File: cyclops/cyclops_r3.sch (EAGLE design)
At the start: 135 parts, among them Q1 BC817, Q2 IRF510, U1 MCP4921, U10 TLV2374, U11 THS4281, U12 MAX4564, U13 ZXTD, U14 ZXTD, U2 ADG3301, U3 MCP4022-50k, U4 LT1931, U5 LT1963A, U6 337L, U7 TLV3701, U8 ADR03, U9 OP1177, X1 SLP3, X2 SLP3, X3 SLP3

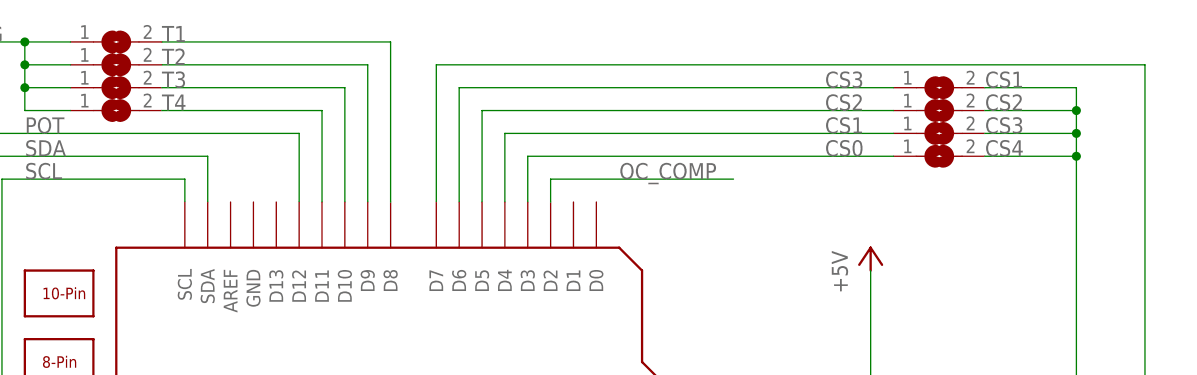
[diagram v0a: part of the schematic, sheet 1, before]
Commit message: Refixed the incorrect labels on the jumper pads.
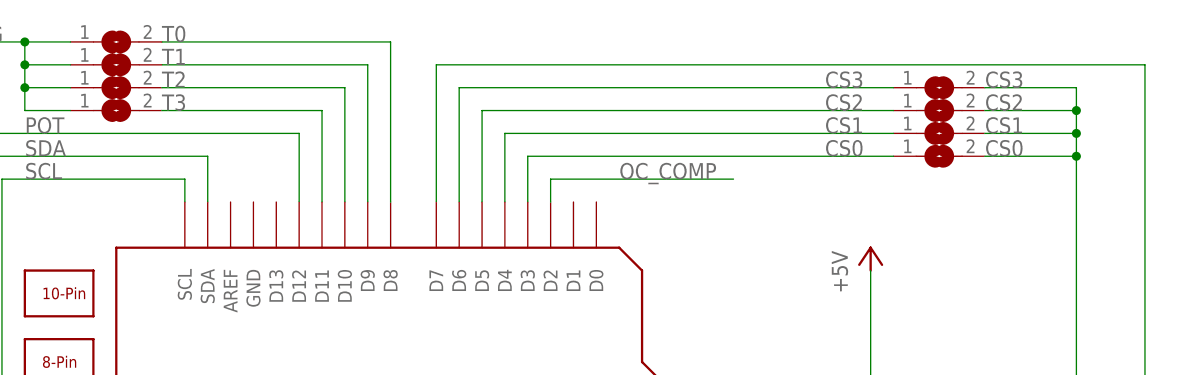
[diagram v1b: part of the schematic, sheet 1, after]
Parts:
- removed T4: (no value), cyclops:SJ
- added T0: (no value), cyclops:SJ
- renumbered CS4 to CS0
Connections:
- net CS1: now also CS1.1; no longer CS3.1
- net CS3: now also CS3.1; no longer CS1.1
- net T0: now also T0.2; no longer T1.2
- net T1: now also T1.2; no longer T2.2
- net T2: now also T2.2; no longer T3.2
- net T3: now also T3.2; no longer T4.2
- net TRIG: now also T0.1; no longer T4.1
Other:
- moved on the sheet: CS1, CS3, T1, T2, T3
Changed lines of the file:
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@@
 <part name="C28" library="cyclops" deviceset="C" device="_0805" value="1uF"/>
 <part name="C26" library="cyclops" deviceset="C" device="_0603" value=".1uF"/>
+<part name="CS3" library="cyclops" deviceset="SJ" device=""/>
+<part name="CS2" library="cyclops" deviceset="SJ" device=""/>
 <part name="CS1" library="cyclops" deviceset="SJ" device=""/>
-<part name="CS2" library="cyclops" deviceset="SJ" device=""/>
-<part name="CS3" library="cyclops" deviceset="SJ" device=""/>
-<part name="CS4" library="cyclops" deviceset="SJ" device=""/>
+<part name="CS0" library="cyclops" deviceset="SJ" device=""/>
 <part name="Q1" library="cyclops" deviceset="BC817*" device="SMD" technology="-16" value="BC817"/>
 <part name="R14" library="cyclops" deviceset="R" device="_0603" value="10k"/>
@@
 <part name="P-2" library="cyclops" deviceset="-5V" device="" value="-1.25V"/>
 <part name="R25" library="cyclops" deviceset="R" device="_0603" value="220k"/>
+<part name="T0" library="cyclops" deviceset="SJ" device=""/>
 <part name="T1" library="cyclops" deviceset="SJ" device=""/>
 <part name="T2" library="cyclops" deviceset="SJ" device=""/>
 <part name="T3" library="cyclops" deviceset="SJ" device=""/>
-<part name="T4" library="cyclops" deviceset="SJ" device=""/>
 <part name="TRIG" library="cyclops" deviceset="BNC" device="_V-BITE" value="361V509E"/>
 <part name="U$47" library="cyclops" deviceset="GND1" device=""/>
@@
 <instance part="TEST" gate="G$1" x="203.2" y="48.26" rot="R180"/>
 <instance part="VAUX_OUT" gate="G$1" x="109.22" y="20.32"/>
-<instance part="CS1" gate="1" x="109.22" y="127" smashed="yes">
+<instance part="CS3" gate="1" x="109.22" y="127" smashed="yes">
 <attribute name="NAME" x="114.3" y="127" size="1.778" layer="95"/>
 <attribute name="VALUE" x="106.68" y="123.19" size="1.778" layer="96"/>
@@
 <attribute name="VALUE" x="106.68" y="120.65" size="1.778" layer="96"/>
 </instance>
-<instance part="CS3" gate="1" x="109.22" y="121.92" smashed="yes">
+<instance part="CS1" gate="1" x="109.22" y="121.92" smashed="yes">
 <attribute name="NAME" x="114.3" y="121.92" size="1.778" layer="95"/>
 <attribute name="VALUE" x="106.68" y="118.11" size="1.778" layer="96"/>
 </instance>
-<instance part="CS4" gate="1" x="109.22" y="119.38" smashed="yes">
+<instance part="CS0" gate="1" x="109.22" y="119.38" smashed="yes">
 <attribute name="NAME" x="114.3" y="119.38" size="1.778" layer="95"/>
 <attribute name="VALUE" x="106.68" y="115.57" size="1.778" layer="96"/>
@@
 <instance part="U$42" gate="G$1" x="172.72" y="58.42"/>
 <instance part="U$43" gate="G$1" x="195.58" y="58.42"/>
-<instance part="T1" gate="1" x="17.78" y="132.08" smashed="yes">
+<instance part="T0" gate="1" x="17.78" y="132.08" smashed="yes">
 <attribute name="NAME" x="22.86" y="132.08" size="1.778" layer="95"/>
 <attribute name="VALUE" x="15.24" y="128.27" size="1.778" layer="96"/>
 </instance>
-<instance part="T2" gate="1" x="17.78" y="129.54" smashed="yes">
+<instance part="T1" gate="1" x="17.78" y="129.54" smashed="yes">
 <attribute name="NAME" x="22.86" y="129.54" size="1.778" layer="95"/>
 <attribute name="VALUE" x="15.24" y="125.73" size="1.778" layer="96"/>
 </instance>
-<instance part="T3" gate="1" x="17.78" y="127" smashed="yes">
+<instance part="T2" gate="1" x="17.78" y="127" smashed="yes">
 <attribute name="NAME" x="22.86" y="127" size="1.778" layer="95"/>
 <attribute name="VALUE" x="15.24" y="123.19" size="1.778" layer="96"/>
 </instance>
-<instance part="T4" gate="1" x="17.78" y="124.46" smashed="yes">
+<instance part="T3" gate="1" x="17.78" y="124.46" smashed="yes">
 <attribute name="NAME" x="22.86" y="124.46" size="1.778" layer="95"/>
 <attribute name="VALUE" x="15.24" y="120.65" size="1.778" layer="96"/>
@@
 <segment>
 <label x="96.52" y="119.38" size="1.778" layer="95"/>
-<pinref part="CS4" gate="1" pin="1"/>
+<pinref part="CS0" gate="1" pin="1"/>
 <pinref part="LEONARDO" gate="G$1" pin="D3"/>
 <wire x1="63.5" y1="119.38" x2="104.14" y2="119.38" width="0.1524" layer="91"/>
@@
 <segment>
 <label x="96.52" y="121.92" size="1.778" layer="95"/>
-<pinref part="CS3" gate="1" pin="1"/>
+<pinref part="CS1" gate="1" pin="1"/>
 <pinref part="LEONARDO" gate="G$1" pin="D4"/>
 <wire x1="60.96" y1="121.92" x2="104.14" y2="121.92" width="0.1524" layer="91"/>
@@
 <segment>
 <label x="96.52" y="127" size="1.778" layer="95"/>
-<pinref part="CS1" gate="1" pin="1"/>
+<pinref part="CS3" gate="1" pin="1"/>
 <pinref part="LEONARDO" gate="G$1" pin="D6"/>
 <wire x1="55.88" y1="127" x2="104.14" y2="127" width="0.1524" layer="91"/>
@@
 <wire x1="114.3" y1="119.38" x2="124.46" y2="119.38" width="0.1524" layer="91"/>
 <junction x="124.46" y="119.38"/>
-<pinref part="CS4" gate="1" pin="2"/>
+<pinref part="CS0" gate="1" pin="2"/>
+<pinref part="CS1" gate="1" pin="2"/>
+<pinref part="CS2" gate="1" pin="2"/>
 <pinref part="CS3" gate="1" pin="2"/>
-<pinref part="CS2" gate="1" pin="2"/>
-<pinref part="CS1" gate="1" pin="2"/>
 </segment>
 <segment>
@@
 <segment>
 <wire x1="0" y1="132.08" x2="7.62" y2="132.08" width="0.1524" layer="91"/>
+<pinref part="T0" gate="1" pin="1"/>
 <pinref part="T1" gate="1" pin="1"/>
-<pinref part="T2" gate="1" pin="1"/>
 <wire x1="7.62" y1="132.08" x2="12.7" y2="132.08" width="0.1524" layer="91"/>
 <wire x1="12.7" y1="129.54" x2="7.62" y2="129.54" width="0.1524" layer="91"/>
 <wire x1="7.62" y1="129.54" x2="7.62" y2="132.08" width="0.1524" layer="91"/>
 <junction x="7.62" y="132.08"/>
-<pinref part="T3" gate="1" pin="1"/>
+<pinref part="T2" gate="1" pin="1"/>
 <wire x1="12.7" y1="127" x2="7.62" y2="127" width="0.1524" layer="91"/>
 <wire x1="7.62" y1="127" x2="7.62" y2="129.54" width="0.1524" layer="91"/>
 <junction x="7.62" y="129.54"/>
-<pinref part="T4" gate="1" pin="1"/>
+<pinref part="T3" gate="1" pin="1"/>
 <wire x1="12.7" y1="124.46" x2="7.62" y2="124.46" width="0.1524" layer="91"/>
 <wire x1="7.62" y1="124.46" x2="7.62" y2="127" width="0.1524" layer="91"/>
@@
 <net name="T0" class="0">
 <segment>
-<pinref part="T1" gate="1" pin="2"/>
+<pinref part="T0" gate="1" pin="2"/>
 <wire x1="22.86" y1="132.08" x2="48.26" y2="132.08" width="0.1524" layer="91"/>
 <pinref part="LEONARDO" gate="G$1" pin="D8"/>
@@
 <net name="T1" class="0">
 <segment>
-<pinref part="T2" gate="1" pin="2"/>
+<pinref part="T1" gate="1" pin="2"/>
 <wire x1="22.86" y1="129.54" x2="45.72" y2="129.54" width="0.1524" layer="91"/>
 <pinref part="LEONARDO" gate="G$1" pin="D9"/>
@@
 <net name="T2" class="0">
 <segment>
-<pinref part="T3" gate="1" pin="2"/>
+<pinref part="T2" gate="1" pin="2"/>
 <wire x1="22.86" y1="127" x2="43.18" y2="127" width="0.1524" layer="91"/>
 <pinref part="LEONARDO" gate="G$1" pin="D10"/>
@@
 <net name="T3" class="0">
 <segment>
-<pinref part="T4" gate="1" pin="2"/>
+<pinref part="T3" gate="1" pin="2"/>
 <wire x1="22.86" y1="124.46" x2="40.64" y2="124.46" width="0.1524" layer="91"/>
 <pinref part="LEONARDO" gate="G$1" pin="D11"/>

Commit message: BOM simplification.
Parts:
- C4: device cyclops:C_0805 -> cyclops:C_1206
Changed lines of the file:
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@@
 <part name="LEONARDO" library="cyclops" deviceset="LEONARDO_R3_ICSP" device="" value="LEONARDO_R3_ICSP"/>
 <part name="U1" library="cyclops" deviceset="MCP4921" device="SOIC" value="MCP4921"/>
-<part name="C4" library="cyclops" deviceset="C" device="_0805" value="10uF"/>
+<part name="C4" library="cyclops" deviceset="C" device="_1206" value="10uF"/>
 <part name="C5" library="cyclops" deviceset="C" device="_0603" value=".1uF"/>
 <part name="C6" library="cyclops" deviceset="C" device="_0805" value="1uF"/>

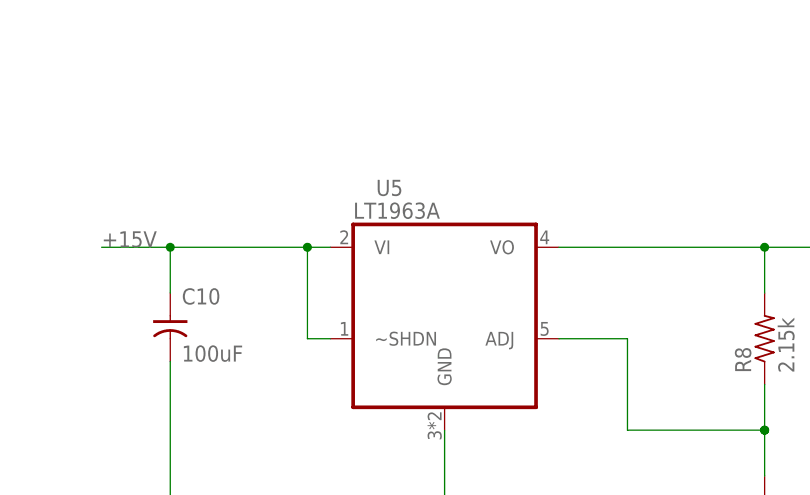
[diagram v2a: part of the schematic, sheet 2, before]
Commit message: Replaced LT1963 with LT1764 to increase current capabilites.
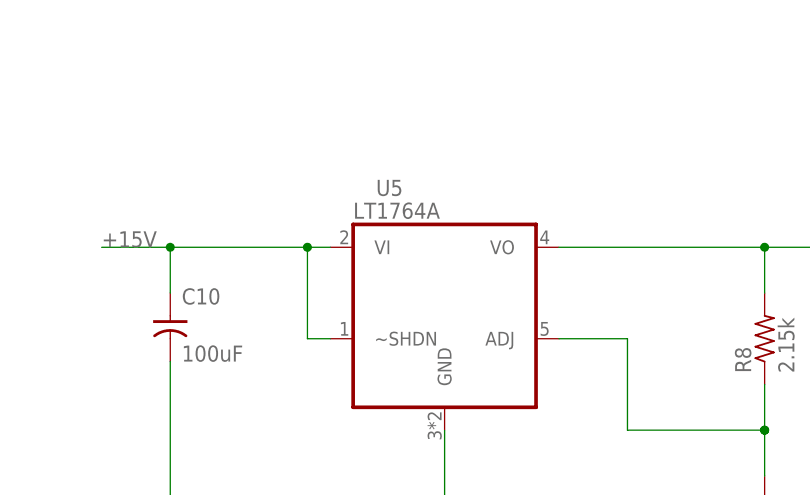
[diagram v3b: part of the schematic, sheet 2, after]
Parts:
- U5: value LT1963A -> LT1764A
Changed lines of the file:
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@@
 <part name="U$53" library="cyclops" deviceset="GND2" device=""/>
 <part name="U$11" library="cyclops" deviceset="GND2" device=""/>
-<part name="U5" library="cyclops" deviceset="LT1963" device="_DDPAK" value="LT1963A"/>
+<part name="U5" library="cyclops" deviceset="LT1963" device="_DDPAK" value="LT1764A"/>
 <part name="C10" library="cyclops" deviceset="C-POL" device="_0807" value="100uF"/>
 <part name="C13" library="cyclops" deviceset="C-POL" device="_0807" value="100uF"/>

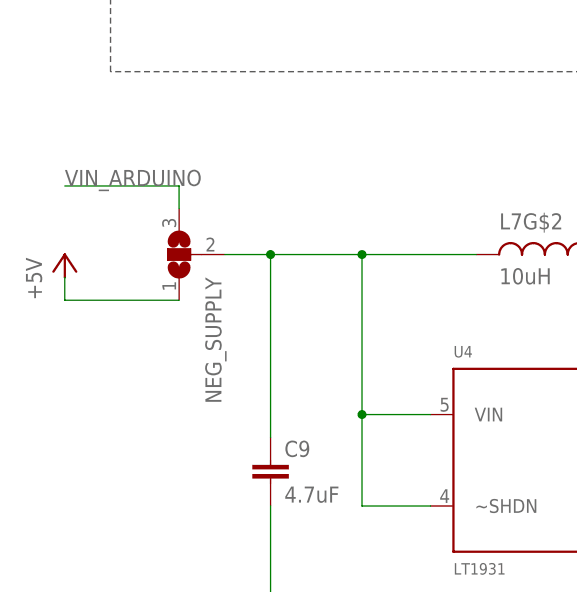
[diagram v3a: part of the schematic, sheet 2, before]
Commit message: Got rid of negative supply source jumper.
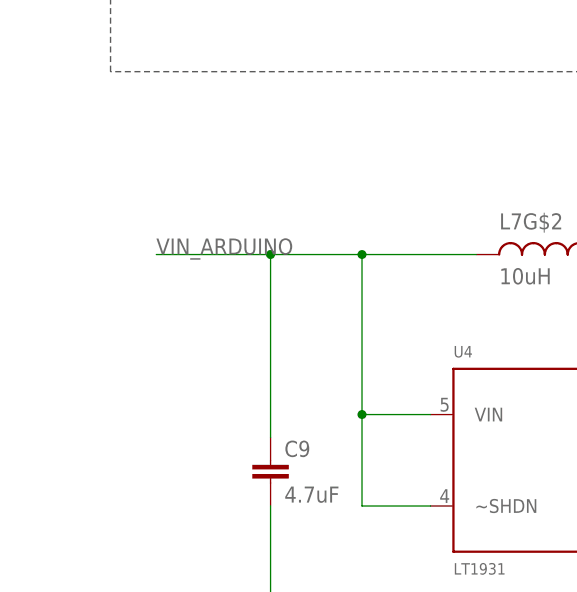
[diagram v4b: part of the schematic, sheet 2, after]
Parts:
- removed NEG_SUPPLY: (no value), cyclops:SJ2W
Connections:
- removed net VIN: C9.1, L7G$2.2, NEG_SUPPLY.2, U4.VIN, U4.~SHDN
- net +5V: no longer NEG_SUPPLY.1
- net VIN_ARDUINO: now also C9.1, L7G$2.2, U4.VIN, U4.~SHDN; no longer NEG_SUPPLY.3
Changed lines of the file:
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@@
 <part name="U$52" library="cyclops" deviceset="GND2" device=""/>
 <part name="P+13" library="cyclops" deviceset="+5V" device="" value="+5V"/>
-<part name="NEG_SUPPLY" library="cyclops" deviceset="SJ2W" device=""/>
-<part name="P+15" library="cyclops" deviceset="+5V" device="" value="+5V"/>
 <part name="C9" library="cyclops" deviceset="C" device="_1206" value="4.7uF"/>
 <part name="U$9" library="cyclops" deviceset="GND2" device=""/>
@@
 <attribute name="NAME" x="58.42" y="-72.39" size="1.778" layer="95" rot="R180"/>
 </instance>
-<instance part="NEG_SUPPLY" gate="G$1" x="-88.9" y="-66.04" smashed="yes" rot="R180">
-<attribute name="NAME" x="-85.979" y="-68.58" size="1.778" layer="95" rot="R270"/>
-<attribute name="VALUE" x="-91.44" y="-64.135" size="1.778" layer="96" rot="R180"/>
-</instance>
-<instance part="P+15" gate="1" x="-101.6" y="-66.04"/>
 <instance part="C9" gate="C" x="-78.74" y="-88.9"/>
 <instance part="U5" gate="G$1" x="-38.1" y="38.1"/>
@@
 </segment>
 </net>
-<net name="VIN" class="0">
+<net name="VIN_ARDUINO" class="0">
 <segment>
 <pinref part="U4" gate="G$1" pin="VIN"/>
@@
 <pinref part="U4" gate="G$1" pin="~SHDN"/>
 <wire x1="-68.58" y1="-93.98" x2="-60.96" y2="-93.98" width="0.1524" layer="91"/>
-<wire x1="-83.82" y1="-66.04" x2="-78.74" y2="-66.04" width="0.1524" layer="91"/>
 <wire x1="-78.74" y1="-66.04" x2="-68.58" y2="-66.04" width="0.1524" layer="91"/>
 <wire x1="-78.74" y1="-86.36" x2="-78.74" y2="-66.04" width="0.1524" layer="91"/>
@@
 <wire x1="-68.58" y1="-66.04" x2="-55.88" y2="-66.04" width="0.1524" layer="91"/>
 <junction x="-68.58" y="-66.04"/>
-<pinref part="NEG_SUPPLY" gate="G$1" pin="2"/>
 <pinref part="C9" gate="C" pin="1"/>
-</segment>
-</net>
-<net name="+5V" class="0">
-<segment>
-<pinref part="NEG_SUPPLY" gate="G$1" pin="1"/>
-<wire x1="-88.9" y1="-71.12" x2="-101.6" y2="-71.12" width="0.1524" layer="91"/>
-<wire x1="-101.6" y1="-71.12" x2="-101.6" y2="-68.58" width="0.1524" layer="91"/>
-</segment>
-</net>
-<net name="VIN_ARDUINO" class="0">
-<segment>
-<pinref part="NEG_SUPPLY" gate="G$1" pin="3"/>
-<wire x1="-88.9" y1="-60.96" x2="-88.9" y2="-58.42" width="0.1524" layer="91"/>
-<wire x1="-88.9" y1="-58.42" x2="-101.6" y2="-58.42" width="0.1524" layer="91"/>
-<label x="-101.6" y="-58.42" size="1.778" layer="95"/>
-</segment>
-</net>
+<wire x1="-78.74" y1="-66.04" x2="-91.44" y2="-66.04" width="0.1524" layer="91"/>
+<label x="-91.44" y="-66.04" size="1.778" layer="95"/>
+</segment>
+</net>

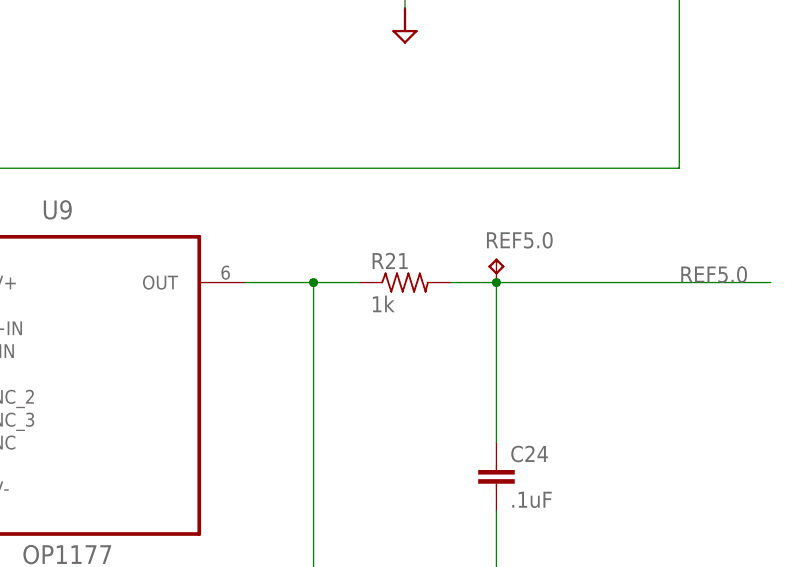
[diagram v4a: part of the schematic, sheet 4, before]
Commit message: Fixed reference voltage issues.
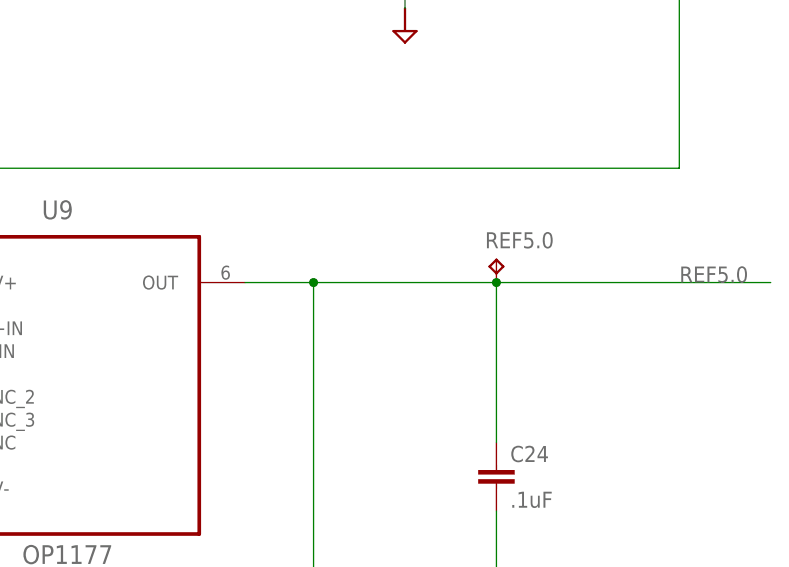
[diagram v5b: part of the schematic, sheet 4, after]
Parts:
- removed R21: 1k, cyclops:R_0603
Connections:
- removed net VREFA2X1: R18.1, R21.1, U9.OUT
- net REF5.0: now also R18.1, U9.OUT; no longer R21.2
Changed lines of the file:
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@@
 <part name="R17" library="cyclops" deviceset="R" device="_0603" value="1k"/>
 <part name="R18" library="cyclops" deviceset="R" device="_0603" value="1k"/>
-<part name="R21" library="cyclops" deviceset="R" device="_0603" value="1k"/>
 <part name="C24" library="cyclops" deviceset="C" device="_0603" value=".1uF"/>
 <part name="U$44" library="cyclops" deviceset="GND2" device=""/>
@@
 <instance part="R17" gate="R" x="-40.64" y="-137.16" rot="R270"/>
 <instance part="R18" gate="R" x="-2.54" y="-121.92" rot="R180"/>
-<instance part="R21" gate="R" x="35.56" y="-83.82"/>
 <instance part="C24" gate="C" x="45.72" y="-104.14"/>
 <instance part="U$44" gate="G$1" x="-40.64" y="-154.94"/>
@@
 </segment>
 </net>
-<net name="VREFA2X1" class="0">
-<segment>
-<wire x1="25.4" y1="-83.82" x2="30.48" y2="-83.82" width="0.1524" layer="91"/>
-<pinref part="R18" gate="R" pin="1"/>
-<wire x1="2.54" y1="-121.92" x2="25.4" y2="-121.92" width="0.1524" layer="91"/>
-<wire x1="25.4" y1="-121.92" x2="25.4" y2="-83.82" width="0.1524" layer="91"/>
-<pinref part="R21" gate="R" pin="1"/>
-<pinref part="U9" gate="A" pin="OUT"/>
-<wire x1="17.78" y1="-83.82" x2="25.4" y2="-83.82" width="0.1524" layer="91"/>
-<junction x="25.4" y="-83.82"/>
-</segment>
-</net>
 <net name="N$18" class="0">
 <segment>
@@
 <net name="REF5.0" class="0">
 <segment>
-<pinref part="R21" gate="R" pin="2"/>
+<pinref part="R18" gate="R" pin="1"/>
+<wire x1="2.54" y1="-121.92" x2="25.4" y2="-121.92" width="0.1524" layer="91"/>
+<wire x1="25.4" y1="-121.92" x2="25.4" y2="-83.82" width="0.1524" layer="91"/>
+<pinref part="U9" gate="A" pin="OUT"/>
+<wire x1="17.78" y1="-83.82" x2="25.4" y2="-83.82" width="0.1524" layer="91"/>
+<junction x="25.4" y="-83.82"/>
 <pinref part="C24" gate="C" pin="1"/>
-<wire x1="40.64" y1="-83.82" x2="45.72" y2="-83.82" width="0.1524" layer="91"/>
 <wire x1="45.72" y1="-83.82" x2="45.72" y2="-101.6" width="0.1524" layer="91"/>
 <wire x1="45.72" y1="-83.82" x2="76.2" y2="-83.82" width="0.1524" layer="91"/>
@@
 <label x="66.04" y="-83.82" size="1.778" layer="95"/>
 <pinref part="REF5.0" gate="G$1" pin="TP"/>
-</segment>
-</net>
+<wire x1="25.4" y1="-83.82" x2="45.72" y2="-83.82" width="0.1524" layer="91"/>
+</segment>
+</net>
